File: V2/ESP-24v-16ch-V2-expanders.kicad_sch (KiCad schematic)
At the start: 8 parts, among them U25 MCP23017_SS, U26 MCP23017_SS, U27 MCP23017_SS

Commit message: Add interrupt pins
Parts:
- removed R32, R34: 1k/62,5mW/0402, Tales:R_0402_1005Metric, symbol Device:R_US
- removed U26, U27: MCP23017_SS, Package_SO:SSOP-28_5.3x10.2mm_P0.65mm, symbol Interface_Expansion:MCP23017_SS
- renumbered R33 to R32
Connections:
- net MCP1-INTB: now reaches U25.19 (INTB)
- net MCP1-INTA: now reaches U25.20 (INTA)
- net MCP2-INTB: now reaches U27.19 (INTB)
- net MCP2-INTA: now reaches U27.20 (INTA)
- no-connect marks 8 -> 0
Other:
- note removed: "INPUTS ADDRESS 0x21"
- note removed: "OUTPUTS ADDRESS 0x23"
- moved on the sheet: R31, R32

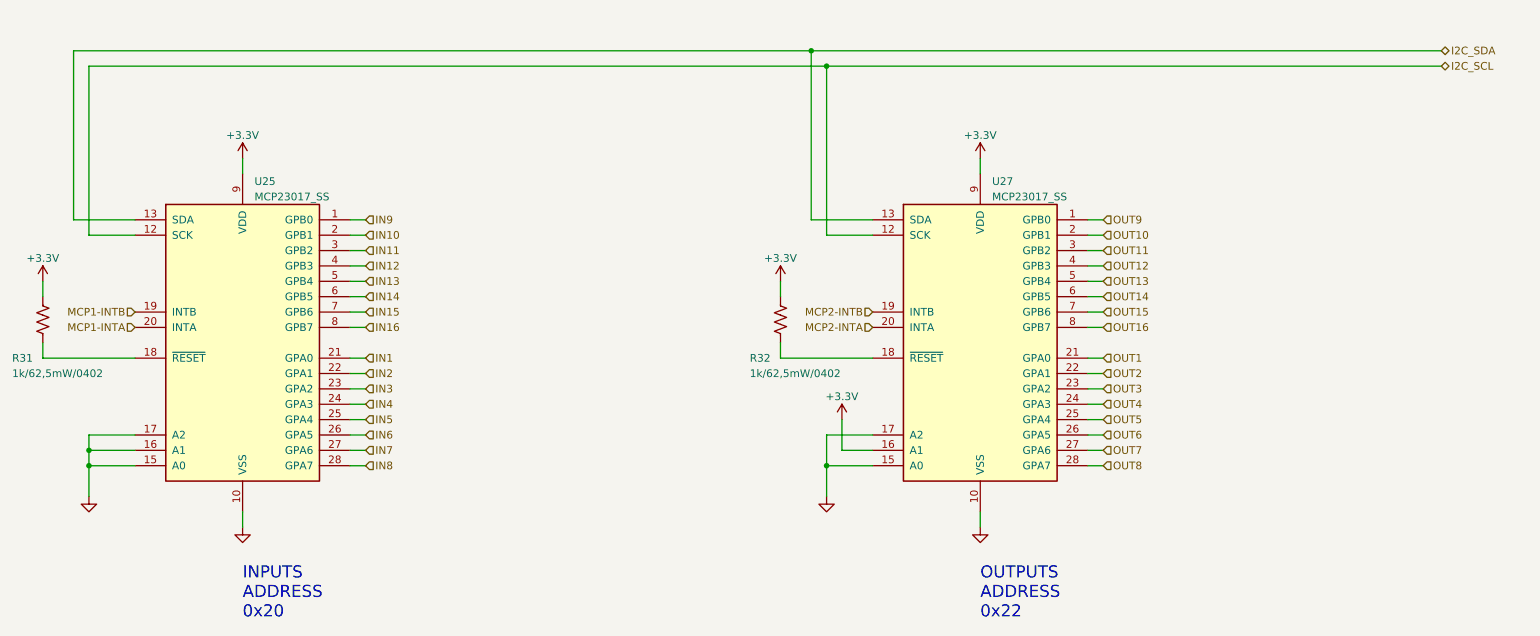
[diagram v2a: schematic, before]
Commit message: MCP interrupt signals routed
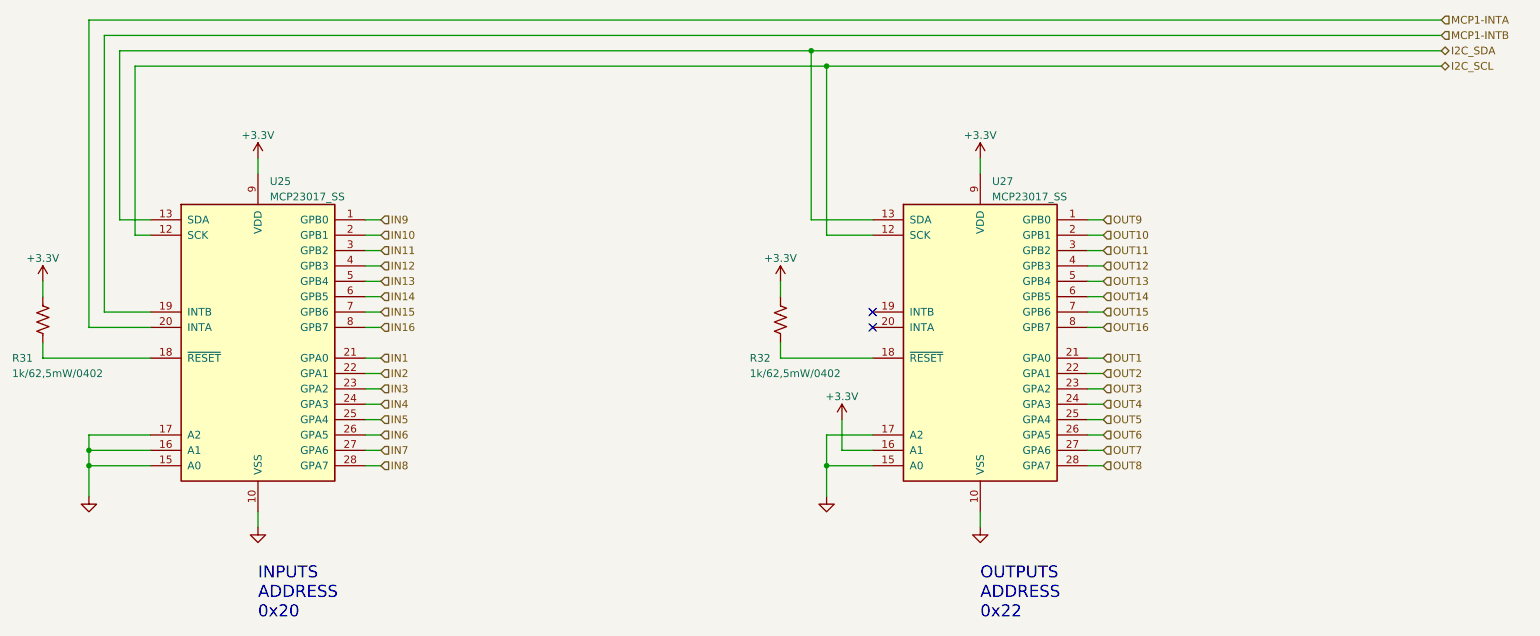
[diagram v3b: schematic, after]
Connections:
- net MCP2-INTA: no longer names the net of U27.20 (INTA)
- net MCP2-INTB: no longer names the net of U27.19 (INTB)
- no-connect marks 0 -> 2
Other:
- moved on the sheet: U25

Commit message: Update documentation in the schematics
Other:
- title: (none) -> ESP 16x 24VDC Input 16x 24VDC Output Module
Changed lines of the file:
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@@
 (kicad_sch (version 20230121) (generator eeschema)
   (paper "A4")
+  (title_block
+    (title "ESP 16x 24VDC Input 16x 24VDC Output Module")
+    (date "2023-05-05")
+    (rev "V2")
+  )
   (junction (at 154.94 55.88) (diameter 0) (color 0 0 0 0)
   )
